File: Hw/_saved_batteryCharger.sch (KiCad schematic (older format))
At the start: 13 parts, among them J1 Vcc, J2 GND, J3 BAT, J4 GND, U1 MCP73831-2-OT

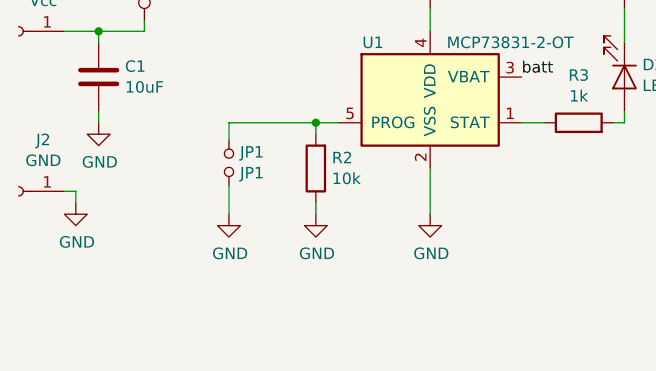
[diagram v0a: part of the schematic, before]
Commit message: Udate jumper for faster charge add logos
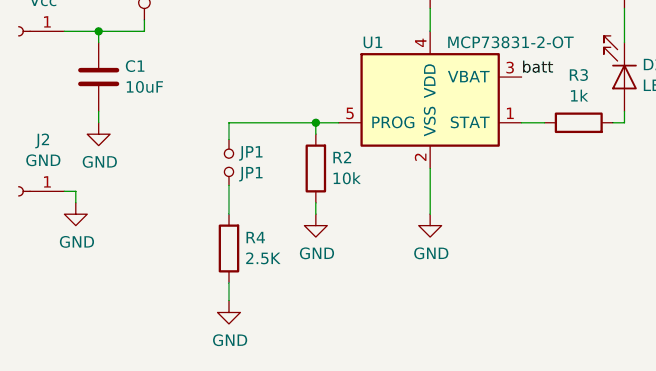
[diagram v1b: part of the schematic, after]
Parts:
- added R4: 2.5K, Resistor_SMD:R_0805_2012Metric_Pad1.15x1.40mm_HandSolder, symbol Device:R
- JP1: footprint (none) -> Jumper:SolderJumper-2_P1.3mm_Open_TrianglePad1.0x1.5mm
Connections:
- net GND: now also R4.1; no longer JP1.2
- new net: JP1.2, R4.2
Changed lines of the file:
@@
 F 0 "JP1" V 5024 3773 50  0000 L CNN
 F 1 "JP1" V 5115 3773 50  0000 L CNN
-F 2 "" H 5070 3725 50  0001 C CNN
+F 2 "Jumper:SolderJumper-2_P1.3mm_Open_TrianglePad1.0x1.5mm" H 5070 3725 50  0001 C CNN
 F 3 "~" H 5070 3725 50  0001 C CNN
 	1    5070 3725
@@
 L power:GND #PWR011
 U 1 1 5D23A033
-P 5070 3950
-F 0 "#PWR011" H 5070 3700 50  0001 C CNN
-F 1 "GND" H 5075 3777 50  0000 C CNN
-F 2 "" H 5070 3950 50  0001 C CNN
-F 3 "" H 5070 3950 50  0001 C CNN
-	1    5070 3950
+P 5070 4330
+F 0 "#PWR011" H 5070 4080 50  0001 C CNN
+F 1 "GND" H 5075 4157 50  0000 C CNN
+F 2 "" H 5070 4330 50  0001 C CNN
+F 3 "" H 5070 4330 50  0001 C CNN
+	1    5070 4330
 	1    0    0    -1
 $EndComp
 Wire Wire Line
 	5070 3950 5070 3825
+$Comp
+L Device:R R4
+U 1 1 5D23B5D2
+P 5070 4100
+F 0 "R4" H 5000 4054 50  0000 R CNN
+F 1 "2.5K" H 5000 4145 50  0000 R CNN
+F 2 "Resistor_SMD:R_0805_2012Metric_Pad1.15x1.40mm_HandSolder" V 5000 4100 50  0001 C CNN
+F 3 "~" H 5070 4100 50  0001 C CNN
+F 4 "ESR10EZPJ103" H 5070 4100 50  0001 C CNN "manf#"
+	1    5070 4100
+	-1   0    0    1
+$EndComp
+Wire Wire Line
+	5070 4330 5070 4250
 $EndSCHEMATC
